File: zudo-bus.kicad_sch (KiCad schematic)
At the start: 0 parts

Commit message: Add Diagram1 power input section with P1/P2 screw terminals
- Add P1 (GND, -12V in) and P2 (+5V in, +12V in) to schematic
- Update circuit-diagrams.mdx with correct pin assignments
- Update BOM with 2-terminal configuration (was 4)
- Add KiCad schematic workflow guidance to CLAUDE.md

Diagram1 establishes power input from external PSU using two
2-position screw terminals instead of four separate terminals.

Co-Authored-By: Claude Opus 4.5 <noreply@anthropic.com>
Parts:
- added P1, P2: WJ500V-5.08-2P-14-00A, easyeda2kicad:CONN-TH_2P-P5.00_WJ500V-5.08-2P, symbol zudo-bus:WJ500V-5.08-2P-14-00A
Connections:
- new net +12V in: P2.2
- new net +5V in: P2.1
- new net -12V in: P1.2
- new net GND: P1.1

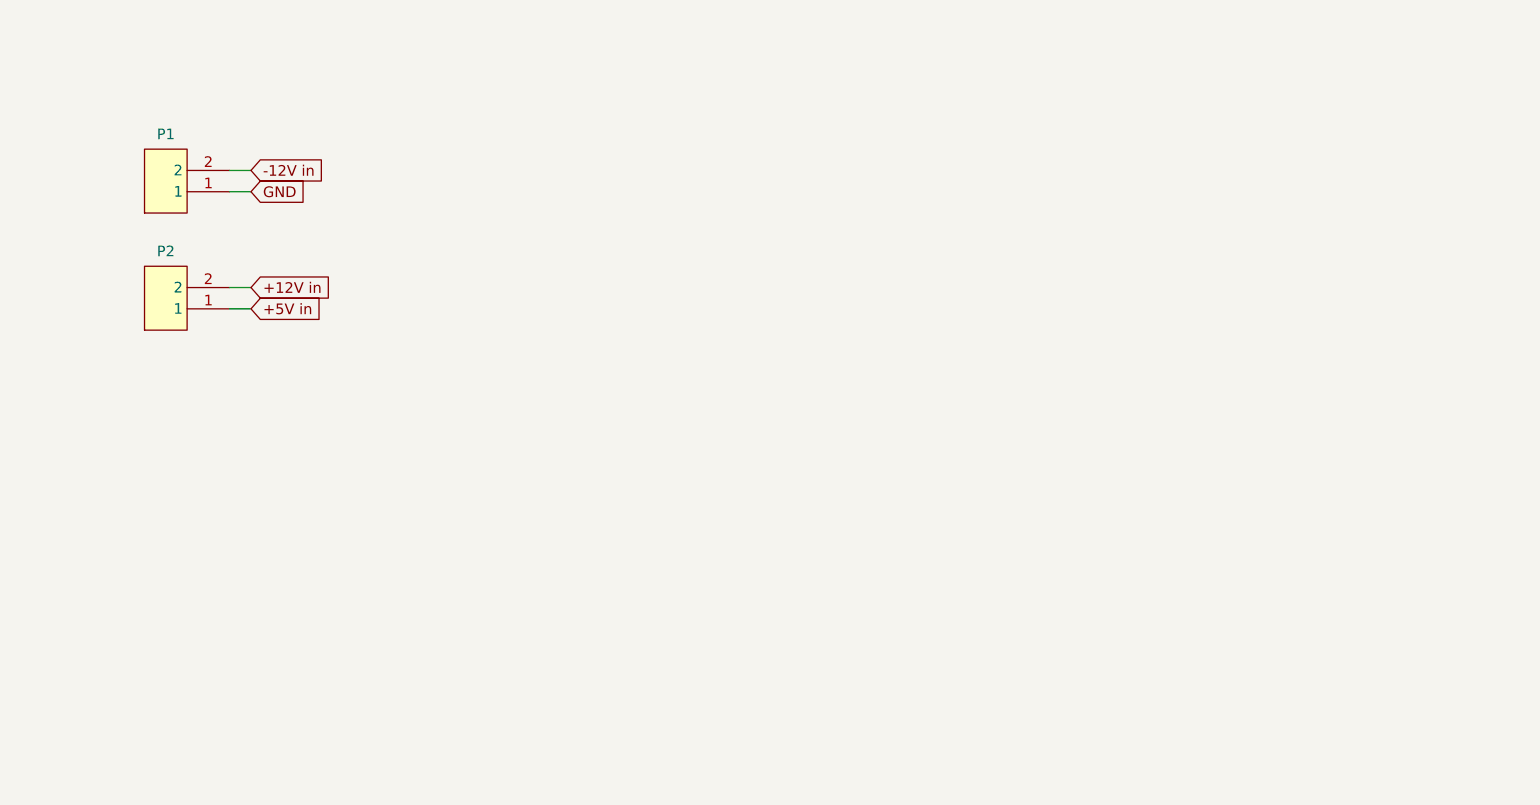
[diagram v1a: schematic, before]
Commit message: Add Diagrams 1-5 to schematic with documentation updates
Diagram1: P1, P2 (power input terminals)
Diagram2: F1, D1 (TVS), D2 (+12V protection)
Diagram3: F2, D3 (TVS), D4 (-12V protection)
Diagram4: F3, D5 (TVS), D6 (+5V protection)
Diagram5: U1 (LDO), D7, D8 (OR-ing), H1 (jumper), C1, C2

- Update circuit-diagrams.mdx with correct component refs
- Add +5V PSU net name (before OR-ing selection)
- Document diode polarity rules for ±12V rails

Co-Authored-By: Claude Opus 4.5 <noreply@anthropic.com>
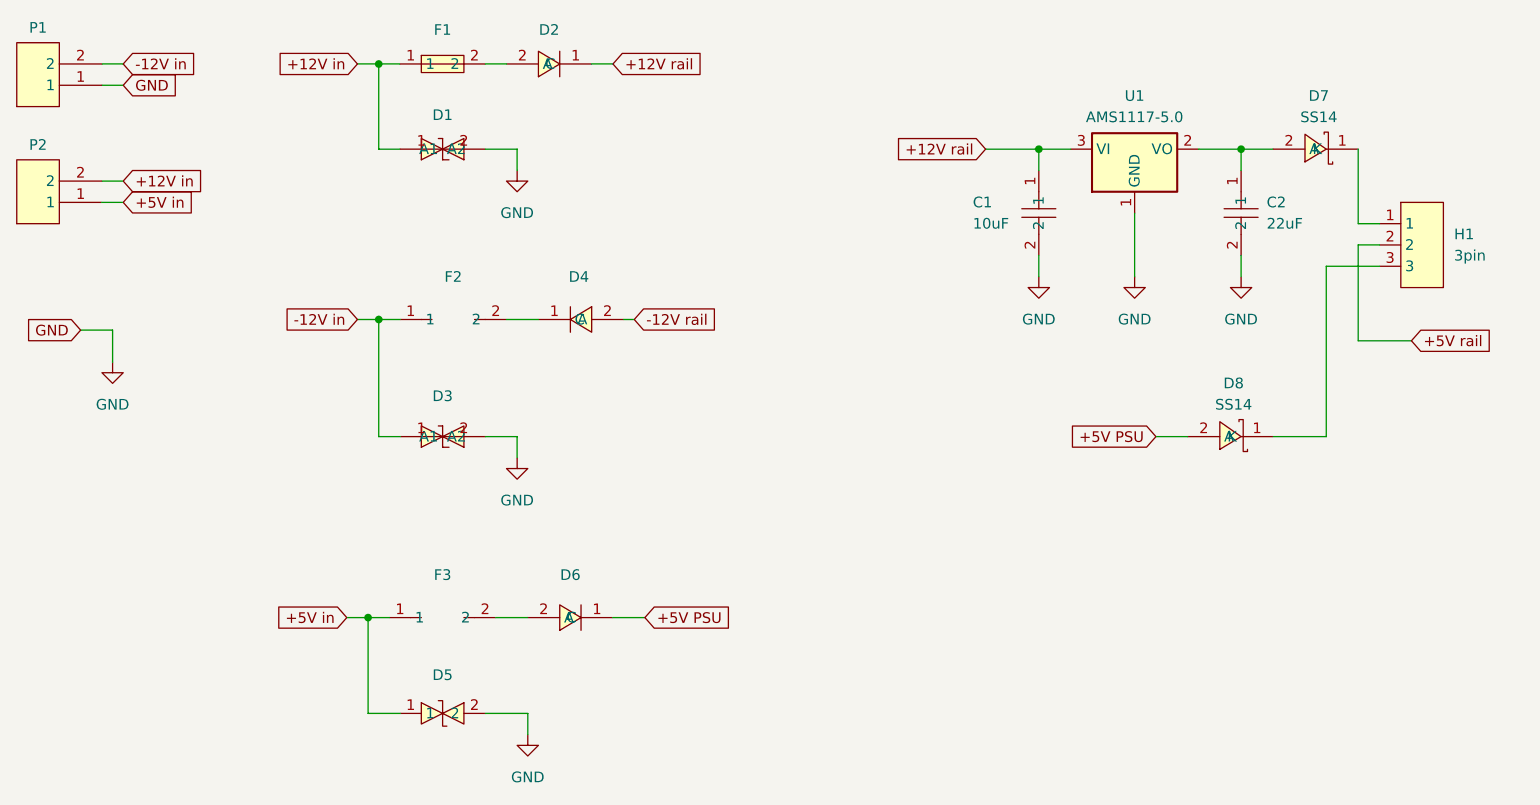
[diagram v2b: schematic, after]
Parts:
- added C1: 10uF, samsung-caps:C0805, symbol samsung-caps:CL21A106KAYNNNE
- added C2: 22uF, samsung-caps:C0805, symbol samsung-caps:CL21A226MAQNNNE
- added D1, D3: SMF12CA_C353317, zudo-bus:SOD-123FL_L2.8-W1.8-LS3.7-BI, symbol zudo-bus-new-protection:SMF12CA_C353317
- added D2, D4, D6: SM4007PL, easyeda2kicad:SOD-123F_L2.8-W1.8-LS3.7-RD, symbol zudo-bus:SM4007PL
- added D5: SMF5.0CA_C908214, :SOD-123_L2.8-W1.8-LS3.7-BI, symbol zudo-bus-protection:SMF5.0CA_C908214
- added D7, D8: SS14, zudo-bus:SMA_L4.2-W2.6-LS5.0-RD_1, symbol zudo-bus-new-protection:SS14
- added F1: BSMD1812-200-30V, :F1812, symbol zudo-bus-protection:BSMD1812-200-30V
- added F2, F3: BSMD1812-150-33V, :F1812, symbol zudo-bus-protection:BSMD1812-150-33V
- added H1: 3pin, easyeda2kicad:HDR-TH_3P-P2.54-V-M-1, symbol zudo-bus:Header-Male-2.54_1x3
- added U1: AMS1117-5.0, Package_TO_SOT_SMD:SOT-223-3_TabPin2, symbol Regulator_Linear:AMS1117-5.0
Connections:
- net +12V in: now also D1.1 (A2), F1.1
- net +5V in: now also D5.1, F3.1
- net -12V in: now also D3.1 (A2), F2.1
- net GND: now also C1.2, C2.2, D1.2 (A1), D3.2 (A1), D5.2, U1.1 (GND)
- new net: C2.1, D7.2 (A), U1.2 (VO)
- new net: D6.2 (A), F3.2
- new net: D7.1 (K), H1.1
- new net: D4.1 (C), F2.2
- new net: D2.2 (A), F1.2
- new net: D8.1 (K), H1.3
- new net +12V rail: C1.1, D2.1 (C), U1.3 (VI)
- new net +5V PSU: D6.1 (C), D8.2 (A)
- new net +5V rail: H1.2
- new net -12V rail: D4.2 (A)
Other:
- moved on the sheet: P1, P2
